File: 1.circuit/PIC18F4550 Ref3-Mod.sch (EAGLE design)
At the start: 17 parts, among them J1 PN61729-S, U1 PIC18F4550_40, X1 20Mhz, X2 2540-

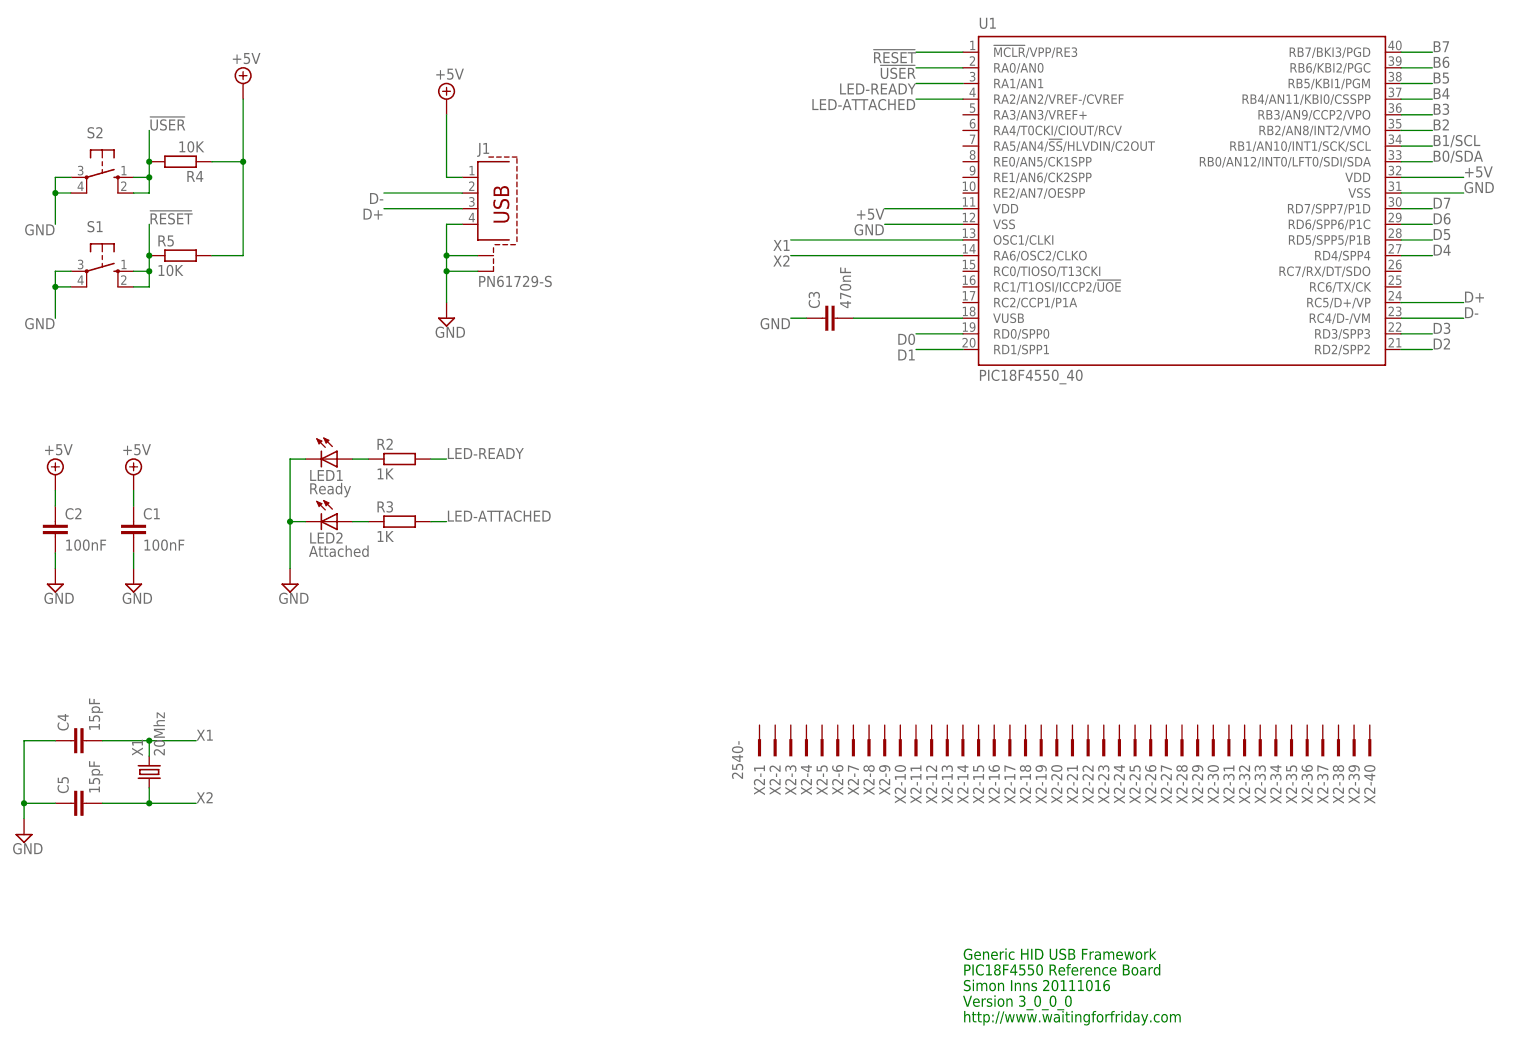
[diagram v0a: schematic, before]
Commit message: adding board, modded schematic
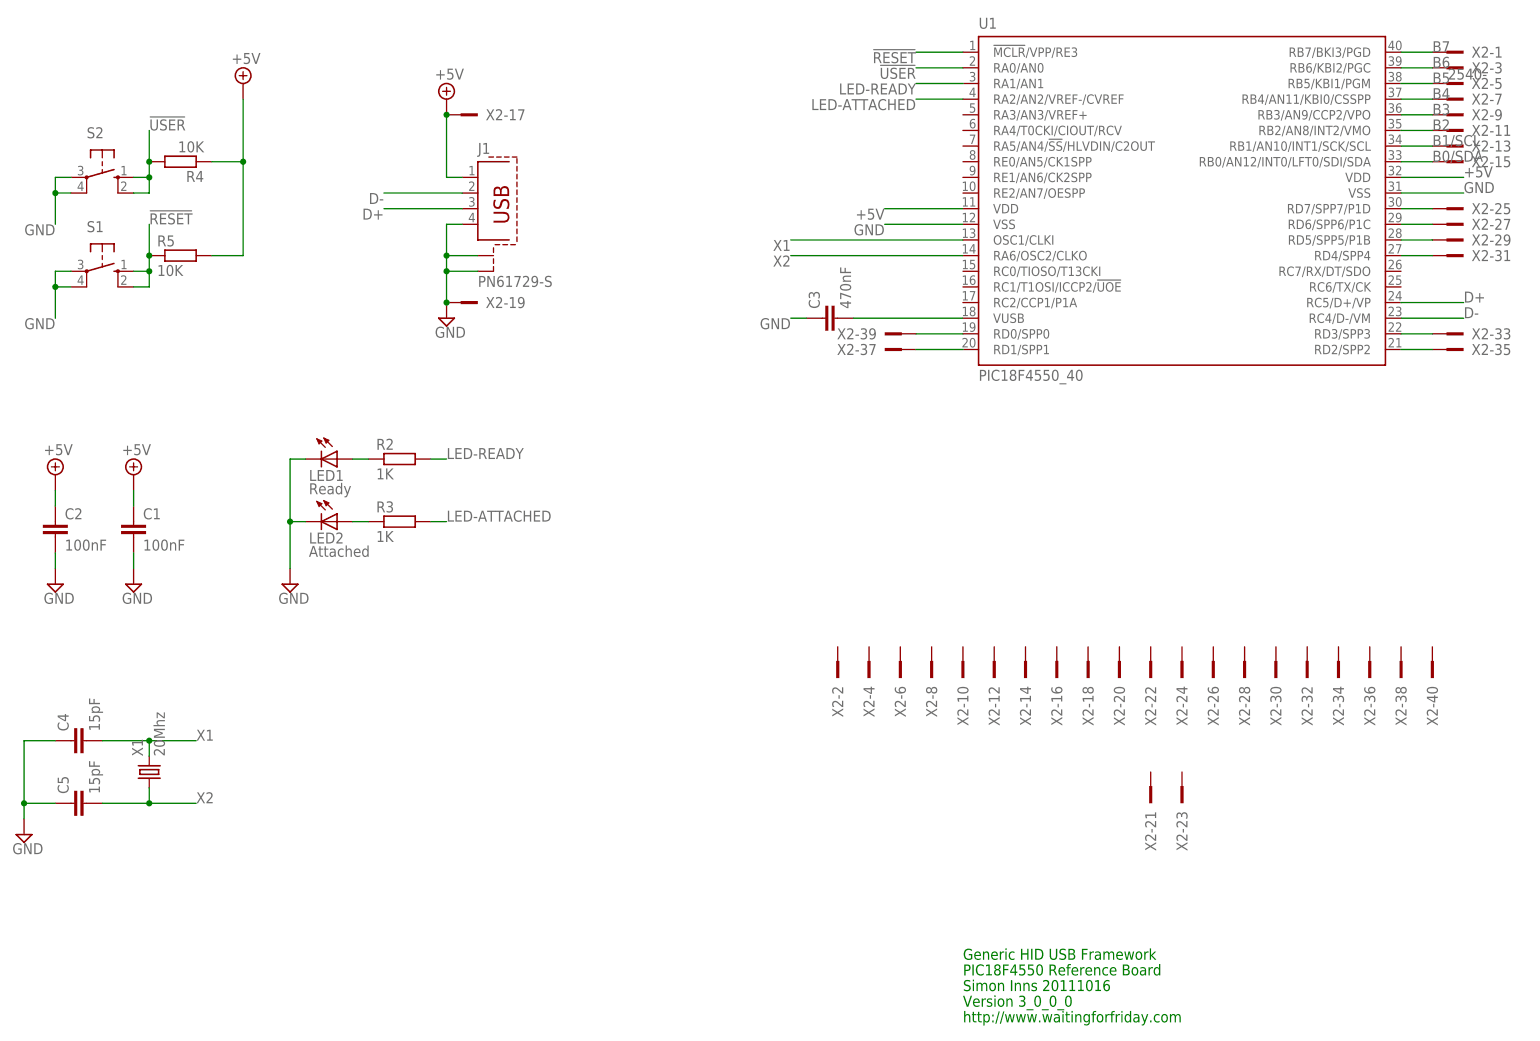
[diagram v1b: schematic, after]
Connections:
- removed net D0: U1.RD0/SPP0
- removed net D1: U1.RD1/SPP1
- removed net D2: U1.RD2/SPP2
- removed net D3: U1.RD3/SPP3
- removed net D4: U1.RD4/SPP4
- removed net D5: U1.RD5/SPP5/P1B
- removed net D6: U1.RD6/SPP6/P1C
- removed net D7: U1.RD7/SPP7/P1D
- new net N$1: U1.RD0/SPP0, X2-39.KL
- new net N$10: U1.RD2/SPP2, X2-35.KL
- new net N$4: U1.RD1/SPP1, X2-37.KL
- new net N$5: U1.RD7/SPP7/P1D, X2-25.KL
- new net N$6: U1.RD6/SPP6/P1C, X2-27.KL
- new net N$7: U1.RD5/SPP5/P1B, X2-29.KL
- new net N$8: U1.RD4/SPP4, X2-31.KL
- new net N$9: U1.RD3/SPP3, X2-33.KL
- net +5V: now also X2-17.KL
- net B0/SDA: now also X2-15.KL
- net B1/SCL: now also X2-13.KL
- net B2: now also X2-11.KL
- net B3: now also X2-9.KL
- net B4: now also X2-7.KL
- net B5: now also X2-5.KL
- net B6: now also X2-3.KL
- net B7: now also X2-1.KL
- net GND: now also X2-19.KL
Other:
- moved on the sheet: X2-1, X2-10, X2-11, X2-12, X2-13, X2-14, X2-15, X2-16, X2-17, X2-18, X2-19, X2-2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
